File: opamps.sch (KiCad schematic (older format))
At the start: 20 parts, among them U501 TSV324IDT, U502 TSV324IDT, U503 TSV324IDT

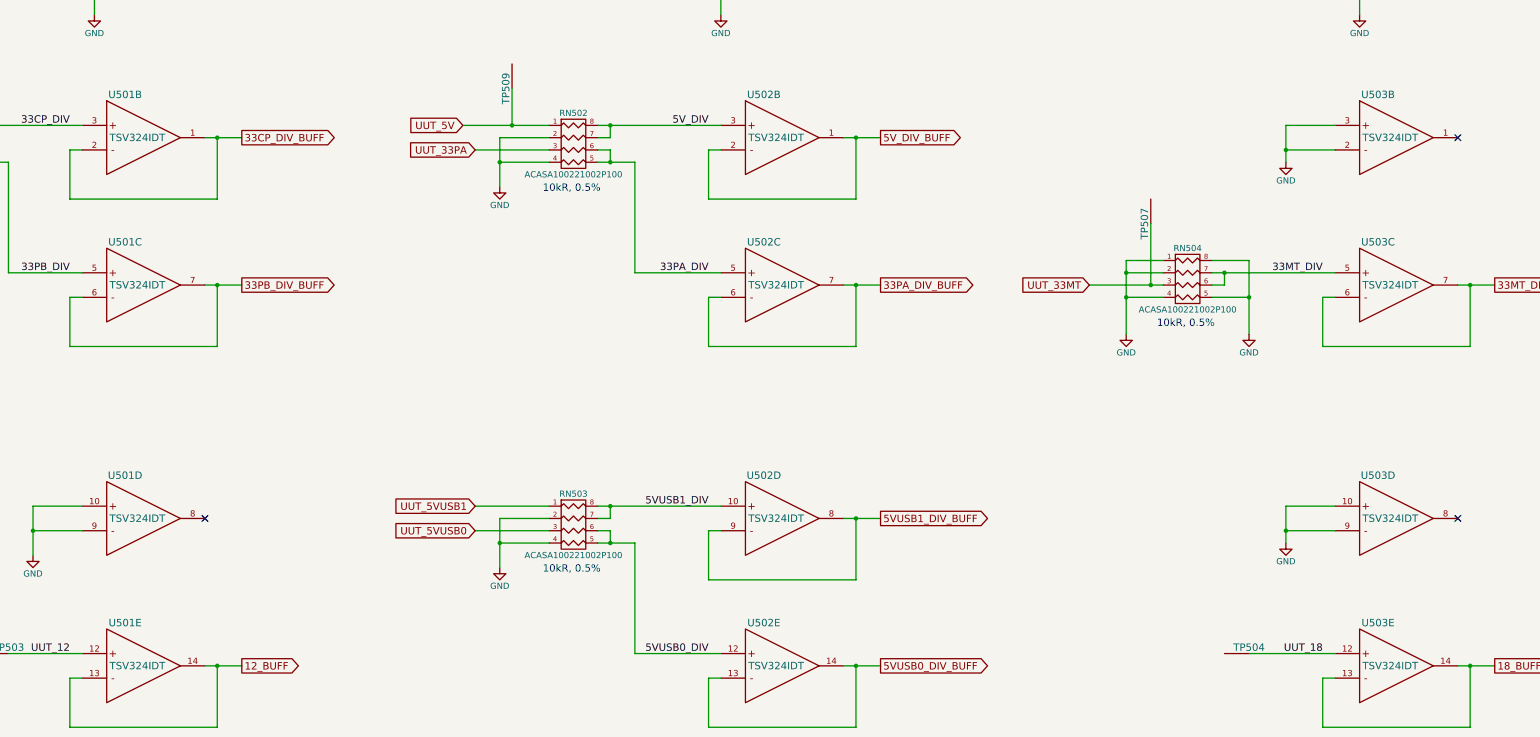
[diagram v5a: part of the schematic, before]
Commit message: opamp rotation
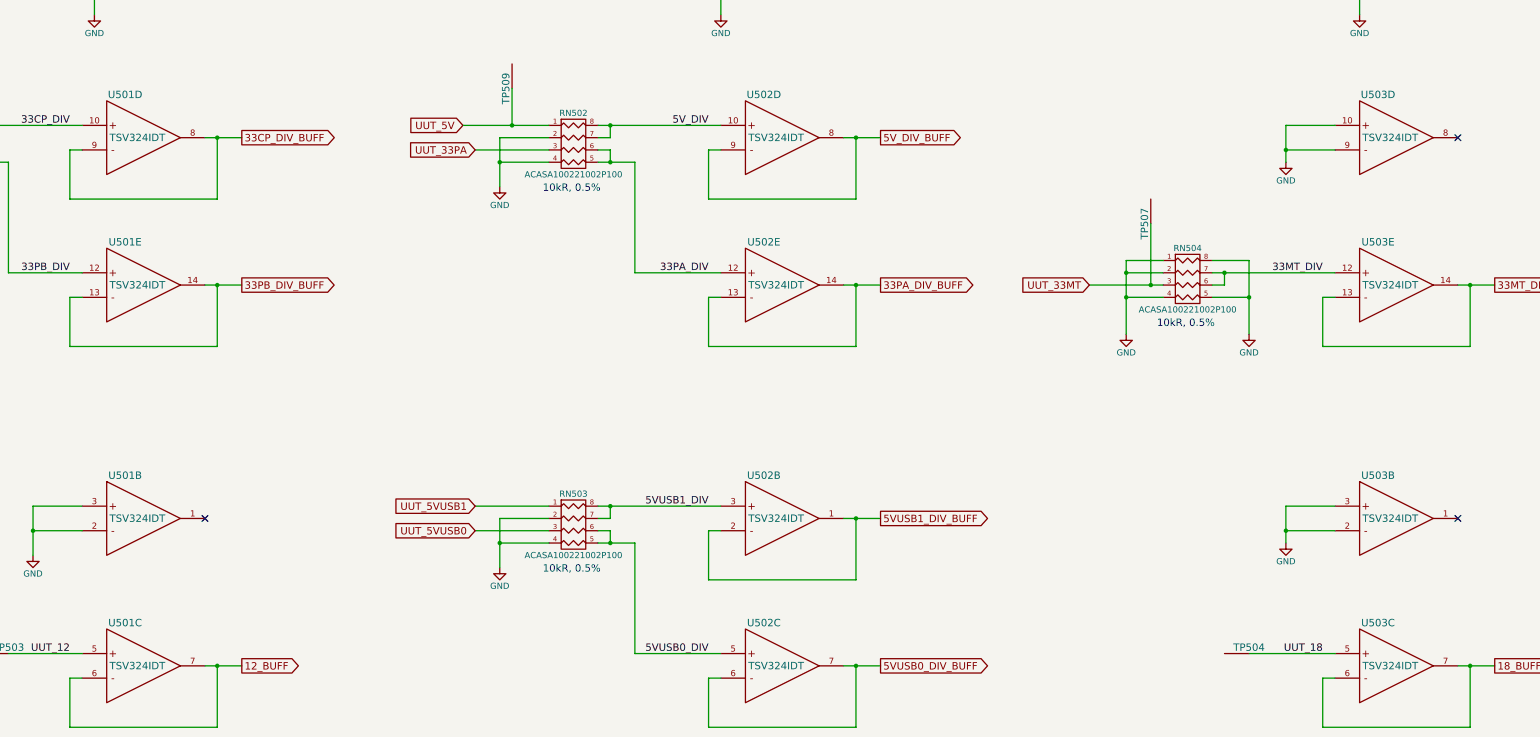
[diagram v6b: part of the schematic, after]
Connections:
- net 12_BUFF: now also U501.6, U501.7; no longer U501.13, U501.14
- net 18_BUFF: now also U503.6, U503.7; no longer U503.13, U503.14
- net 33CP_DIV: now also U501.10; no longer U501.3
- net 33CP_DIV_BUFF: now also U501.8, U501.9; no longer U501.1, U501.2
- net 33MT_DIV: now also U503.12; no longer U503.5
- net 33MT_DIV_BUFF: now also U503.13, U503.14; no longer U503.6, U503.7
- net 33PA_DIV: now also U502.12; no longer U502.5
- net 33PA_DIV_BUFF: now also U502.13, U502.14; no longer U502.6, U502.7
- net 33PB_DIV: now also U501.12; no longer U501.5
- net 33PB_DIV_BUFF: now also U501.13, U501.14; no longer U501.6, U501.7
- net 5VUSB0_DIV: now also U502.5; no longer U502.12
- net 5VUSB0_DIV_BUFF: now also U502.6, U502.7; no longer U502.13, U502.14
- net 5VUSB1_DIV: now also U502.3; no longer U502.10
- net 5VUSB1_DIV_BUFF: now also U502.1, U502.2; no longer U502.8, U502.9
- net 5V_DIV: now also U502.10; no longer U502.3
- net 5V_DIV_BUFF: now also U502.8, U502.9; no longer U502.1, U502.2
- net GND: now also U501.2, U501.3; no longer U501.10, U501.9
- net UUT_12: now also U501.5; no longer U501.12
- net UUT_18: now also U503.5; no longer U503.12
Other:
- moved on the sheet: U501B, U501C, U501D, U501E, U502B, U502C, U502D, U502E, U503B, U503C, U503D, U503E
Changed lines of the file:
@@
 L TSV324IDT U502
 U 5 1 55403A57
-P 9250 8100
-F 0 "U502" H 9150 8450 60  0000 C CNN
-F 1 "TSV324IDT" H 9250 8100 60  0000 C CNN
-F 2 "SMD_Packages:SOIC-14_N" H 9200 8150 60  0001 C CNN
-F 3 "" H 9200 8150 60  0000 C CNN
-	5    9250 8100
+P 9250 5000
+AR Path="/55403A57" Ref="U502"  Part="5"
+AR Path="/55403272/55403A57" Ref="U502"  Part="5"
+F 0 "U502" H 9150 5350 60  0000 C CNN
+F 1 "TSV324IDT" H 9250 5000 60  0000 C CNN
+F 2 "SMD_Packages:SOIC-14_N" H 9200 5050 60  0001 C CNN
+F 3 "" H 9200 5050 60  0000 C CNN
+	5    9250 5000
 	1    0    0    -1
 $EndComp
@@
 L TSV324IDT U501
 U 5 1 55403AF6
-P 4050 8100
-F 0 "U501" H 3950 8450 60  0000 C CNN
-F 1 "TSV324IDT" H 4050 8100 60  0000 C CNN
-F 2 "SMD_Packages:SOIC-14_N" H 4000 8150 60  0001 C CNN
-F 3 "" H 4000 8150 60  0000 C CNN
-	5    4050 8100
+P 4050 5000
+AR Path="/55403AF6" Ref="U501"  Part="5"
+AR Path="/55403272/55403AF6" Ref="U501"  Part="5"
+F 0 "U501" H 3950 5350 60  0000 C CNN
+F 1 "TSV324IDT" H 4050 5000 60  0000 C CNN
+F 2 "SMD_Packages:SOIC-14_N" H 4000 5050 60  0001 C CNN
+F 3 "" H 4000 5050 60  0000 C CNN
+	5    4050 5000
 	1    0    0    -1
 $EndComp
@@
 U 1 1 55406FF8
 P 4400 2200
+AR Path="/55406FF8" Ref="U501"  Part="1"
+AR Path="/55403272/55406FF8" Ref="U501"  Part="1"
 F 0 "U501" H 4300 2550 60  0000 C CNN
 F 1 "TSV324IDT" H 4400 2200 60  0000 C CNN
@@
 U 1 1 5540707E
 P 9500 2200
+AR Path="/5540707E" Ref="U502"  Part="1"
+AR Path="/55403272/5540707E" Ref="U502"  Part="1"
 F 0 "U502" H 9400 2550 60  0000 C CNN
 F 1 "TSV324IDT" H 9500 2200 60  0000 C CNN
@@
 L TSV324IDT U501
 U 2 1 554070C1
+P 4050 6900
+AR Path="/554070C1" Ref="U501"  Part="2"
+AR Path="/55403272/554070C1" Ref="U501"  Part="2"
+F 0 "U501" H 3950 7250 60  0000 C CNN
+F 1 "TSV324IDT" H 4050 6900 60  0000 C CNN
+F 2 "SMD_Packages:SOIC-14_N" H 4000 6950 60  0001 C CNN
+F 3 "" H 4000 6950 60  0000 C CNN
+	2    4050 6900
+	1    0    0    -1
+$EndComp
+$Comp
+L TSV324IDT U502
+U 2 1 55407129
+P 9250 6900
+AR Path="/55407129" Ref="U502"  Part="2"
+AR Path="/55403272/55407129" Ref="U502"  Part="2"
+F 0 "U502" H 9150 7250 60  0000 C CNN
+F 1 "TSV324IDT" H 9250 6900 60  0000 C CNN
+F 2 "SMD_Packages:SOIC-14_N" H 9200 6950 60  0001 C CNN
+F 3 "" H 9200 6950 60  0000 C CNN
+	2    9250 6900
+	1    0    0    -1
+$EndComp
+$Comp
+L TSV324IDT U501
+U 3 1 55407156
+P 4050 8100
+AR Path="/55407156" Ref="U501"  Part="3"
+AR Path="/55403272/55407156" Ref="U501"  Part="3"
+F 0 "U501" H 3950 8450 60  0000 C CNN
+F 1 "TSV324IDT" H 4050 8100 60  0000 C CNN
+F 2 "SMD_Packages:SOIC-14_N" H 4000 8150 60  0001 C CNN
+F 3 "" H 4000 8150 60  0000 C CNN
+	3    4050 8100
+	1    0    0    -1
+$EndComp
+$Comp
+L TSV324IDT U502
+U 3 1 554071E0
+P 9250 8100
+AR Path="/554071E0" Ref="U502"  Part="3"
+AR Path="/55403272/554071E0" Ref="U502"  Part="3"
+F 0 "U502" H 9150 8450 60  0000 C CNN
+F 1 "TSV324IDT" H 9250 8100 60  0000 C CNN
+F 2 "SMD_Packages:SOIC-14_N" H 9200 8150 60  0001 C CNN
+F 3 "" H 9200 8150 60  0000 C CNN
+	3    9250 8100
+	1    0    0    -1
+$EndComp
+$Comp
+L TSV324IDT U501
+U 4 1 55407279
 P 4050 3800
+AR Path="/55407279" Ref="U501"  Part="4"
+AR Path="/55403272/55407279" Ref="U501"  Part="4"
 F 0 "U501" H 3950 4150 60  0000 C CNN
 F 1 "TSV324IDT" H 4050 3800 60  0000 C CNN
 F 2 "SMD_Packages:SOIC-14_N" H 4000 3850 60  0001 C CNN
 F 3 "" H 4000 3850 60  0000 C CNN
-	2    4050 3800
+	4    4050 3800
 	1    0    0    -1
 $EndComp
 $Comp
 L TSV324IDT U502
-U 2 1 55407129
+U 4 1 554072E3
 P 9250 3800
+AR Path="/554072E3" Ref="U502"  Part="4"
+AR Path="/55403272/554072E3" Ref="U502"  Part="4"
 F 0 "U502" H 9150 4150 60  0000 C CNN
 F 1 "TSV324IDT" H 9250 3800 60  0000 C CNN
 F 2 "SMD_Packages:SOIC-14_N" H 9200 3850 60  0001 C CNN
 F 3 "" H 9200 3850 60  0000 C CNN
-	2    9250 3800
-	1    0    0    -1
-$EndComp
-$Comp
-L TSV324IDT U501
-U 3 1 55407156
-P 4050 5000
-F 0 "U501" H 3950 5350 60  0000 C CNN
-F 1 "TSV324IDT" H 4050 5000 60  0000 C CNN
-F 2 "SMD_Packages:SOIC-14_N" H 4000 5050 60  0001 C CNN
-F 3 "" H 4000 5050 60  0000 C CNN
-	3    4050 5000
-	1    0    0    -1
-$EndComp
-$Comp
-L TSV324IDT U502
-U 3 1 554071E0
-P 9250 5000
-F 0 "U502" H 9150 5350 60  0000 C CNN
-F 1 "TSV324IDT" H 9250 5000 60  0000 C CNN
-F 2 "SMD_Packages:SOIC-14_N" H 9200 5050 60  0001 C CNN
-F 3 "" H 9200 5050 60  0000 C CNN
-	3    9250 5000
-	1    0    0    -1
-$EndComp
-$Comp
-L TSV324IDT U501
-U 4 1 55407279
-P 4050 6900
-F 0 "U501" H 3950 7250 60  0000 C CNN
-F 1 "TSV324IDT" H 4050 6900 60  0000 C CNN
-F 2 "SMD_Packages:SOIC-14_N" H 4000 6950 60  0001 C CNN
-F 3 "" H 4000 6950 60  0000 C CNN
-	4    4050 6900
-	1    0    0    -1
-$EndComp
-$Comp
-L TSV324IDT U502
-U 4 1 554072E3
-P 9250 6900
-F 0 "U502" H 9150 7250 60  0000 C CNN
-F 1 "TSV324IDT" H 9250 6900 60  0000 C CNN
-F 2 "SMD_Packages:SOIC-14_N" H 9200 6950 60  0001 C CNN
-F 3 "" H 9200 6950 60  0000 C CNN
-	4    9250 6900
+	4    9250 3800
 	1    0    0    -1
 $EndComp
@@
 L TSV324IDT U503
 U 5 1 5540E503
-P 14250 8100
-F 0 "U503" H 14150 8450 60  0000 C CNN
-F 1 "TSV324IDT" H 14250 8100 60  0000 C CNN
-F 2 "SMD_Packages:SOIC-14_N" H 14200 8150 60  0001 C CNN
-F 3 "" H 14200 8150 60  0000 C CNN
-	5    14250 8100
+P 14250 5000
+AR Path="/5540E503" Ref="U503"  Part="5"
+AR Path="/55403272/5540E503" Ref="U503"  Part="5"
+F 0 "U503" H 14150 5350 60  0000 C CNN
+F 1 "TSV324IDT" H 14250 5000 60  0000 C CNN
+F 2 "SMD_Packages:SOIC-14_N" H 14200 5050 60  0001 C CNN
+F 3 "" H 14200 5050 60  0000 C CNN
+	5    14250 5000
 	1    0    0    -1
 $EndComp
@@
 U 1 1 5540E526
 P 14700 2200
+AR Path="/5540E526" Ref="U503"  Part="1"
+AR Path="/55403272/5540E526" Ref="U503"  Part="1"
 F 0 "U503" H 14600 2550 60  0000 C CNN
 F 1 "TSV324IDT" H 14700 2200 60  0000 C CNN
@@
 L TSV324IDT U503
 U 2 1 5540E52C
-P 14250 3800
-F 0 "U503" H 14150 4150 60  0000 C CNN
-F 1 "TSV324IDT" H 14250 3800 60  0000 C CNN
-F 2 "SMD_Packages:SOIC-14_N" H 14200 3850 60  0001 C CNN
-F 3 "" H 14200 3850 60  0000 C CNN
-	2    14250 3800
+P 14250 6900
+AR Path="/5540E52C" Ref="U503"  Part="2"
+AR Path="/55403272/5540E52C" Ref="U503"  Part="2"
+F 0 "U503" H 14150 7250 60  0000 C CNN
+F 1 "TSV324IDT" H 14250 6900 60  0000 C CNN
+F 2 "SMD_Packages:SOIC-14_N" H 14200 6950 60  0001 C CNN
+F 3 "" H 14200 6950 60  0000 C CNN
+	2    14250 6900
 	1    0    0    -1
 $EndComp
@@
 L TSV324IDT U503
 U 3 1 5540EC41
-P 14250 5000
-F 0 "U503" H 14150 5350 60  0000 C CNN
-F 1 "TSV324IDT" H 14250 5000 60  0000 C CNN
-F 2 "SMD_Packages:SOIC-14_N" H 14200 5050 60  0001 C CNN
-F 3 "" H 14200 5050 60  0000 C CNN
-	3    14250 5000
+P 14250 8100
+AR Path="/5540EC41" Ref="U503"  Part="3"
+AR Path="/55403272/5540EC41" Ref="U503"  Part="3"
+F 0 "U503" H 14150 8450 60  0000 C CNN
+F 1 "TSV324IDT" H 14250 8100 60  0000 C CNN
+F 2 "SMD_Packages:SOIC-14_N" H 14200 8150 60  0001 C CNN
+F 3 "" H 14200 8150 60  0000 C CNN
+	3    14250 8100
 	1    0    0    -1
 $EndComp
@@
 L TSV324IDT U503
 U 4 1 5540ECB0
-P 14250 6900
-F 0 "U503" H 14150 7250 60  0000 C CNN
-F 1 "TSV324IDT" H 14250 6900 60  0000 C CNN
-F 2 "SMD_Packages:SOIC-14_N" H 14200 6950 60  0001 C CNN
-F 3 "" H 14200 6950 60  0000 C CNN
-	4    14250 6900
-	1    0    0    -1
-$EndComp
+P 14250 3800
+AR Path="/5540ECB0" Ref="U503"  Part="4"
+AR Path="/55403272/5540ECB0" Ref="U503"  Part="4"
+F 0 "U503" H 14150 4150 60  0000 C CNN
+F 1 "TSV324IDT" H 14250 3800 60  0000 C CNN
+F 2 "SMD_Packages:SOIC-14_N" H 14200 3850 60  0001 C CNN
+F 3 "" H 14200 3850 60  0000 C CNN
+	4    14250 3800
+	1    0    0    -1
+$EndComp

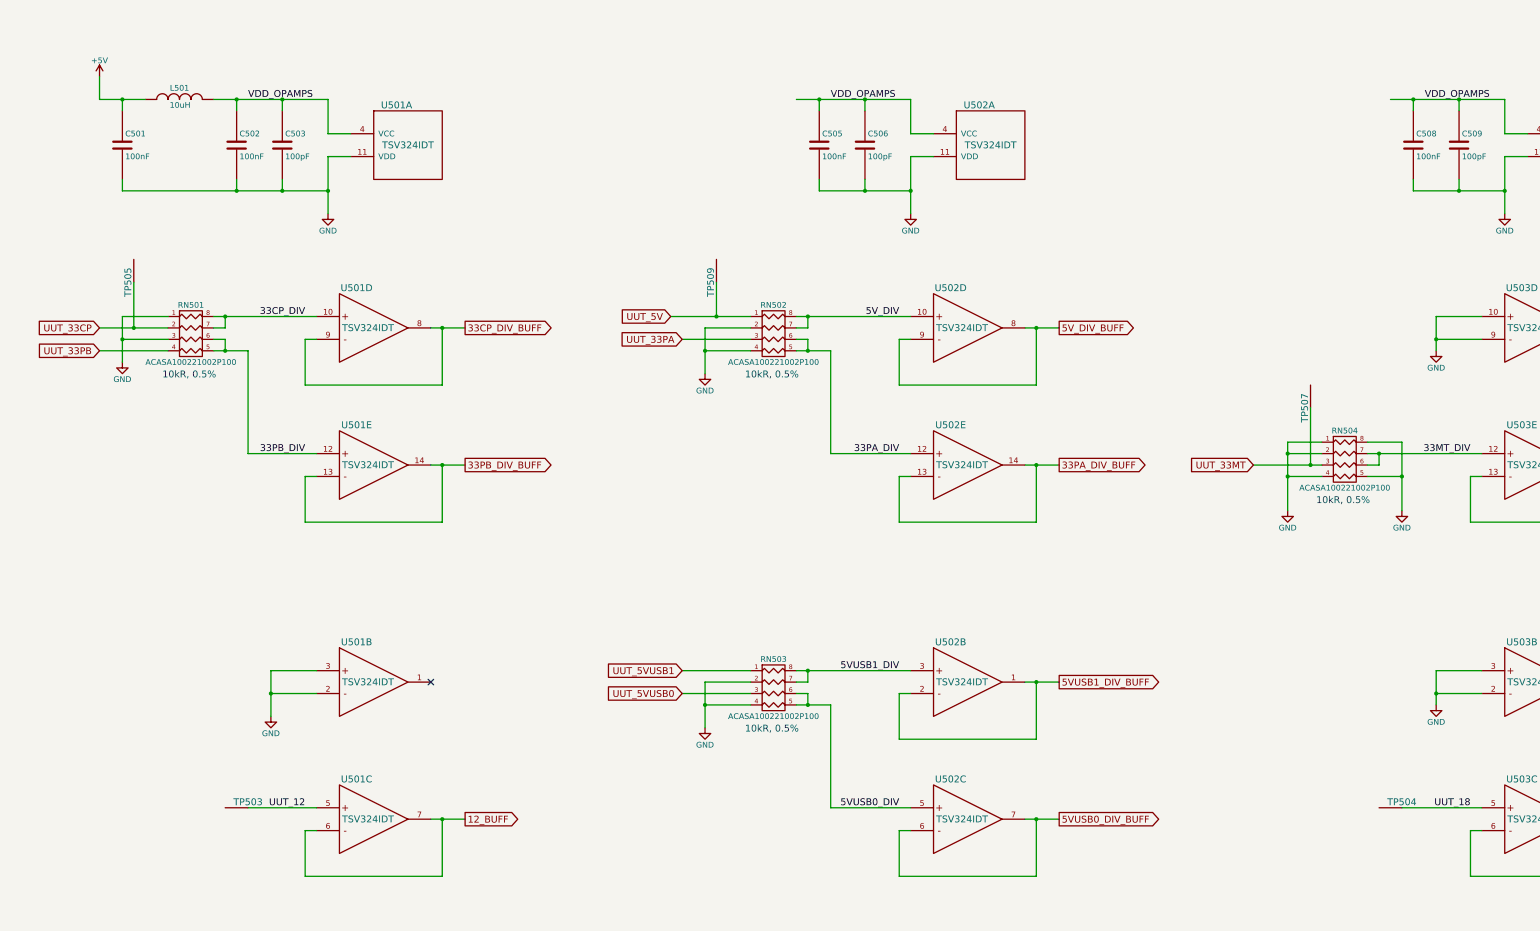
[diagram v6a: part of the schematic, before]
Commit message: pulldowns on 1.2, 1.8 and power swap for opamps
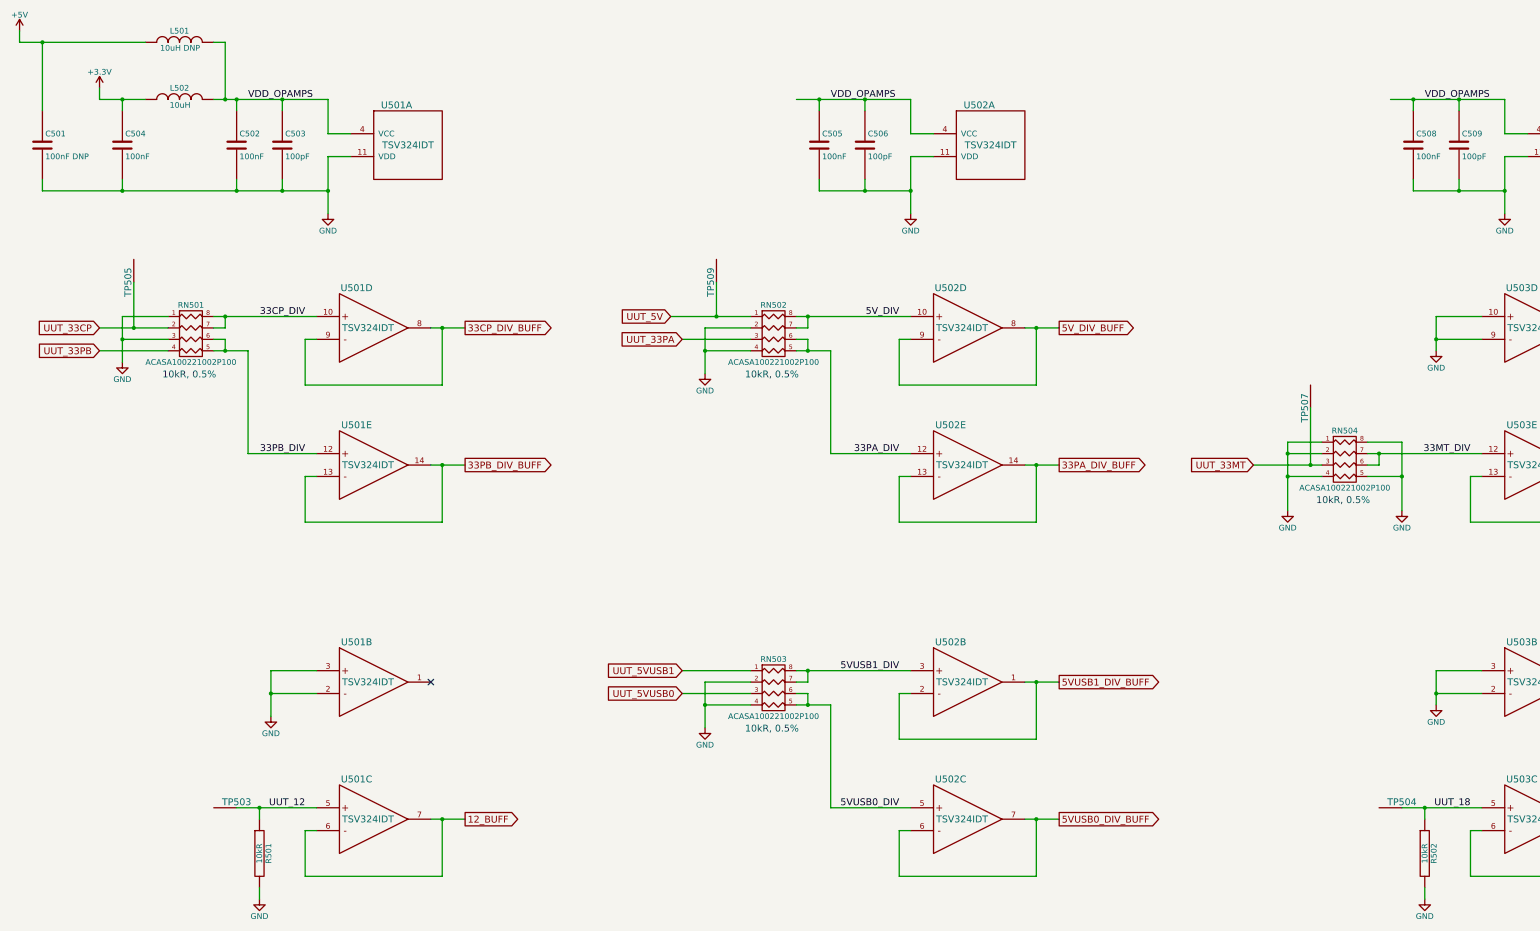
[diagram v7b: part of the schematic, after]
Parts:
- added C504: 100nF, tm-kicad-lib:SMD-0402-C, symbol TM_C
- added L502: 10uH, tm-kicad-lib:SMD-0603-R, symbol TM_L
- added R501, R502: 10kR, tm-kicad-lib:SMD-0402-R, symbol TM_R
- C501: value 100nF -> 100nF DNP
- L501: value 10uH -> 10uH DNP
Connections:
- net GND: now also C504.2, R501.2, R502.2
- net UUT_12: now also R501.1
- net UUT_18: now also R502.1
- net VDD_OPAMPS: now also L502.1
- new net +3V3: C504.1, L502.2
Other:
- moved on the sheet: C501, L501, TP503
